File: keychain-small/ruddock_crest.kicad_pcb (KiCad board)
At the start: 2 copper layers, 38.1 x 45.7 mm, 4 parts

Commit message: Migrate to KiCad 5.1.4
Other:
- outline, holes or cut-outs redrawn
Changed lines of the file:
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@@
-(kicad_pcb (version 20171130) (host pcbnew "(5.0.1)-3")
+(kicad_pcb (version 20171130) (host pcbnew "(5.1.4)-1")
   (general
     (thickness 1.6)
@@
     (zone_45_only no)
     (trace_min 0.2)
-    (segment_width 0.5)
-    (edge_width 0.1)
     (via_size 0.8)
     (via_drill 0.4)
@@
     (uvia_min_size 0.2)
     (uvia_min_drill 0.1)
+    (edge_width 0.1)
+    (segment_width 0.5)
     (pcb_text_width 0.3)
     (pcb_text_size 1.5 1.5)
@@
       (xy 0.287869 -18.341347)) (layer F.Cu) (width 0.01))
   )
+  (gr_arc (start 140.97 107.95) (end 133.466674 90.423999) (angle -313.6458442) (layer Edge.Cuts) (width 0.1))
   (gr_arc (start 150.510695 85.344) (end 148.300896 90.576399) (angle 67.1) (layer B.SilkS) (width 0.5))
   (gr_arc (start 150.495 85.344) (end 148.285201 90.576399) (angle 67.1) (layer F.SilkS) (width 0.5))
@@
   (gr_arc (start 131.445 85.344) (end 133.984999 90.423999) (angle -63.4) (layer B.SilkS) (width 0.5))
   (gr_arc (start 131.445 85.344) (end 133.984999 90.423999) (angle -63.4) (layer F.SilkS) (width 0.5))
-  (gr_arc (start 140.97 107.95) (end 133.477001 90.424001) (angle -313.703074) (layer Edge.Cuts) (width 0.1))
-  (gr_arc (start 150.495 85.344) (end 148.463001 90.423999) (angle 68.2) (layer Edge.Cuts) (width 0.1))
+  (gr_arc (start 150.505326 85.344134) (end 148.473327 90.424133) (angle 68.2) (layer Edge.Cuts) (width 0.1))
   (gr_circle (center 150.495 85.344) (end 150.368 85.344) (layer Dwgs.User) (width 0.1))
   (gr_circle (center 150.495 85.344) (end 145.034 85.344) (layer Dwgs.User) (width 0.1))
-  (gr_arc (start 131.445 85.344) (end 133.476999 90.423999) (angle -68.19859051) (layer Edge.Cuts) (width 0.1))
+  (gr_arc (start 131.434674 85.343999) (end 133.466673 90.423998) (angle -68.19859051) (layer Edge.Cuts) (width 0.1))
   (gr_circle (center 131.445 85.344) (end 131.572 85.344) (layer Dwgs.User) (width 0.1))
   (gr_circle (center 131.445 85.344) (end 136.906 85.344) (layer Dwgs.User) (width 0.1))

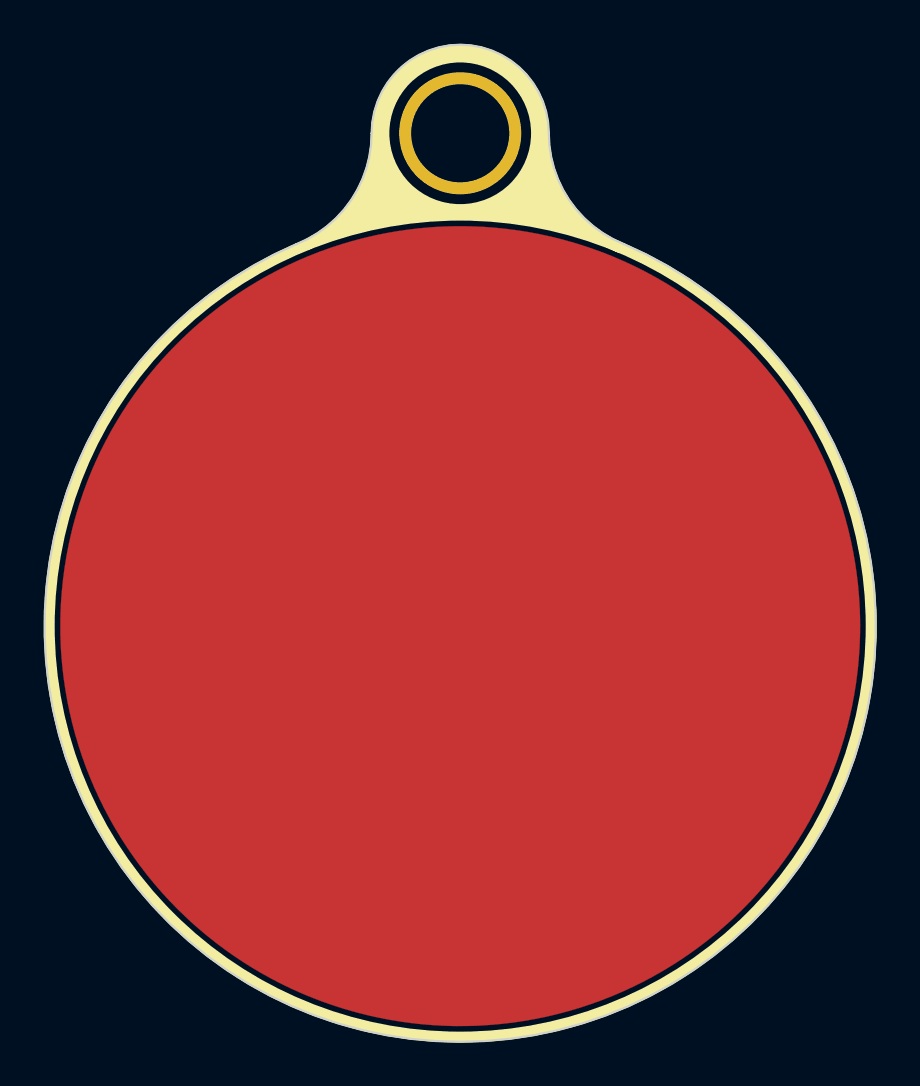
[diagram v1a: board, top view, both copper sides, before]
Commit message: Replace copper crest pad with fill zones
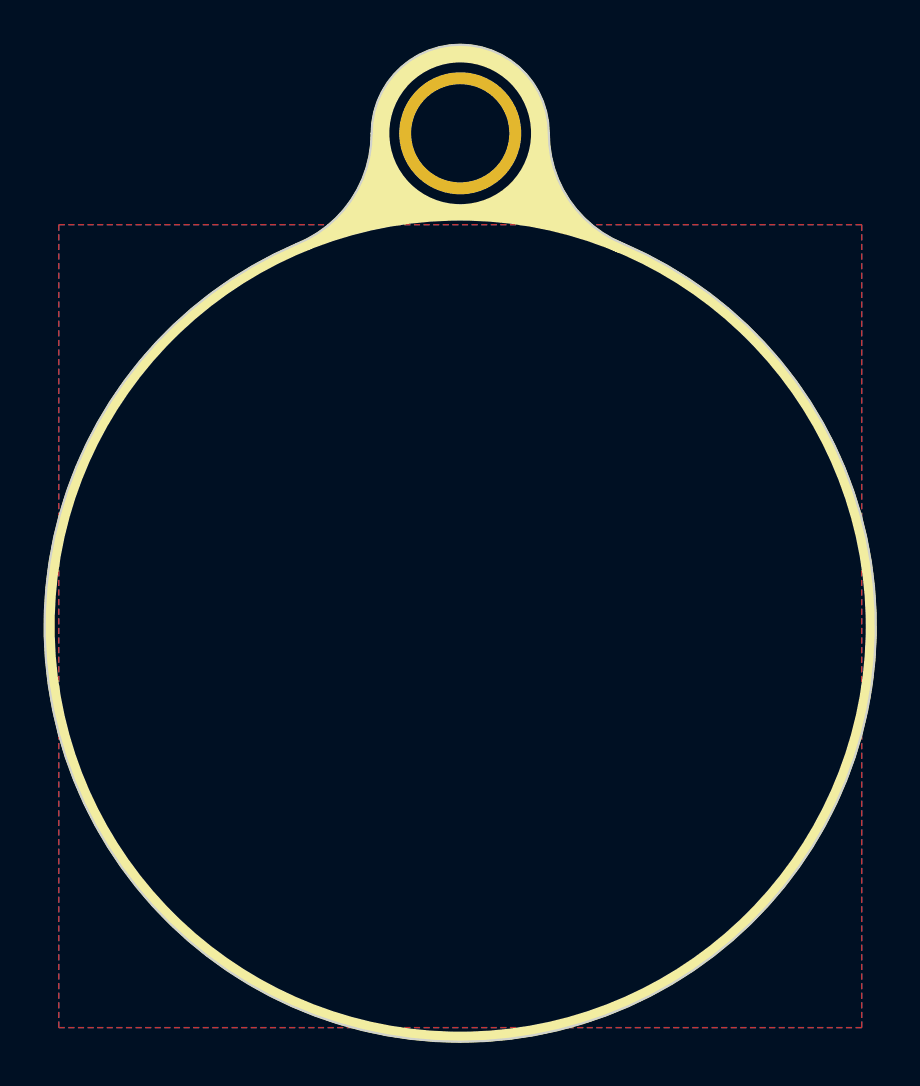
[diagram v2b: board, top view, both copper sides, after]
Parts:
- removed the G*** at (141.0, 108.0)
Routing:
- added copper zone on B.Cu, net (none)
- added copper zone on F.Cu, net (none)
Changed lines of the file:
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@@
     (tracks 0)
     (zones 0)
-    (modules 4)
+    (modules 3)
     (nets 1)
   )
@@
       (xy 9.730745 -13.40817) (xy 9.745385 -13.421618) (xy 9.978417 -13.636419) (xy 10.013345 -13.51111)) (layer F.Mask) (width 0.01))
   )
-  (module crest:circle_cu_1in5 (layer F.Cu)
-    (at 140.97 107.95)
-    (fp_text reference G*** (at 0 0) (layer F.SilkS) hide
-      (effects (font (size 1.524 1.524) (thickness 0.3)))
-    )
-    (fp_text value LOGO (at 0.75 0) (layer F.SilkS) hide
-      (effects (font (size 1.524 1.524) (thickness 0.3)))
-    )
-    (fp_poly (pts (xy 0.287869 -18.341347) (xy 0.628456 -18.333307) (xy 0.961238 -18.319252) (xy 1.067536 -18.313358)
-      (xy 1.586336 -18.275505) (xy 2.102502 -18.223229) (xy 2.615773 -18.156636) (xy 3.125887 -18.075837)
-      (xy 3.632583 -17.980939) (xy 4.135602 -17.872049) (xy 4.63468 -17.749278) (xy 5.129559 -17.612732)
-      (xy 5.619975 -17.46252) (xy 6.10567 -17.29875) (xy 6.58638 -17.121531) (xy 7.061847 -16.930971)
-      (xy 7.531807 -16.727178) (xy 7.996001 -16.51026) (xy 8.454168 -16.280326) (xy 8.906046 -16.037484)
-      (xy 9.351375 -15.781841) (xy 9.789892 -15.513508) (xy 10.221339 -15.232591) (xy 10.645453 -14.939199)
-      (xy 11.061973 -14.63344) (xy 11.470638 -14.315423) (xy 11.871188 -13.985255) (xy 12.208452 -13.692138)
-      (xy 12.383032 -13.534063) (xy 12.563152 -13.366008) (xy 12.746398 -13.190385) (xy 12.930358 -13.009606)
-      (xy 13.11262 -12.826085) (xy 13.290771 -12.642233) (xy 13.462399 -12.460464) (xy 13.62509 -12.28319)
-      (xy 13.692138 -12.208453) (xy 14.033691 -11.813903) (xy 14.363246 -11.41087) (xy 14.680696 -10.999533)
-      (xy 14.985936 -10.580068) (xy 15.278857 -10.152652) (xy 15.559353 -9.717464) (xy 15.827317 -9.274679)
-      (xy 16.082642 -8.824475) (xy 16.325222 -8.367031) (xy 16.554949 -7.902522) (xy 16.771718 -7.431126)
-      (xy 16.97542 -6.95302) (xy 17.165949 -6.468382) (xy 17.189629 -6.405218) (xy 17.364087 -5.916258)
-      (xy 17.524449 -5.423109) (xy 17.67067 -4.925995) (xy 17.802701 -4.425139) (xy 17.920497 -3.920765)
-      (xy 18.024008 -3.413097) (xy 18.11319 -2.90236) (xy 18.187993 -2.388777) (xy 18.248372 -1.872571)
-      (xy 18.294279 -1.353968) (xy 18.313357 -1.067537) (xy 18.329376 -0.738224) (xy 18.339381 -0.399719)
-      (xy 18.343371 -0.056272) (xy 18.341346 0.287869) (xy 18.333306 0.628456) (xy 18.319251 0.961238)
-      (xy 18.313357 1.067536) (xy 18.275504 1.586336) (xy 18.223228 2.102502) (xy 18.156636 2.615773)
-      (xy 18.075836 3.125887) (xy 17.980938 3.632583) (xy 17.872049 4.135602) (xy 17.749277 4.63468)
-      (xy 17.612731 5.129559) (xy 17.462519 5.619975) (xy 17.298749 6.10567) (xy 17.12153 6.58638)
-      (xy 16.93097 7.061847) (xy 16.727177 7.531807) (xy 16.510259 7.996001) (xy 16.280325 8.454168)
-      (xy 16.037483 8.906046) (xy 15.781841 9.351375) (xy 15.513507 9.789892) (xy 15.23259 10.221339)
-      (xy 14.939198 10.645453) (xy 14.633439 11.061973) (xy 14.315422 11.470638) (xy 13.985254 11.871188)
-      (xy 13.692138 12.208452) (xy 13.534062 12.383032) (xy 13.366007 12.563152) (xy 13.190384 12.746398)
-      (xy 13.009605 12.930358) (xy 12.826084 13.11262) (xy 12.642232 13.290771) (xy 12.460463 13.462399)
-      (xy 12.283189 13.62509) (xy 12.208452 13.692138) (xy 11.814467 14.033183) (xy 11.411954 14.362284)
-      (xy 11.001147 14.679318) (xy 10.582275 14.98416) (xy 10.155572 15.276688) (xy 9.721268 15.55678)
-      (xy 9.279596 15.824312) (xy 8.830786 16.079161) (xy 8.37507 16.321204) (xy 7.91268 16.550318)
-      (xy 7.443848 16.76638) (xy 6.968805 16.969268) (xy 6.487783 17.158858) (xy 6.001014 17.335027)
-      (xy 5.508728 17.497652) (xy 5.011159 17.64661) (xy 4.508536 17.781779) (xy 4.505739 17.782489)
-      (xy 4.005732 17.901871) (xy 3.502761 18.007024) (xy 2.996576 18.097984) (xy 2.486931 18.174786)
-      (xy 1.973579 18.237465) (xy 1.456271 18.286059) (xy 0.934759 18.320601) (xy 0.688034 18.331996)
-      (xy 0.640369 18.333612) (xy 0.580731 18.335179) (xy 0.511147 18.336678) (xy 0.433639 18.338086)
-      (xy 0.350234 18.339384) (xy 0.262955 18.340551) (xy 0.173826 18.341565) (xy 0.084873 18.342407)
-      (xy -0.00188 18.343055) (xy -0.084409 18.343489) (xy -0.160688 18.343687) (xy -0.228695 18.34363)
-      (xy -0.286403 18.343296) (xy -0.331789 18.342665) (xy -0.338667 18.342515) (xy -0.769418 18.328007)
-      (xy -1.192714 18.305017) (xy -1.607212 18.273641) (xy -2.011574 18.233973) (xy -2.245508 18.206637)
-      (xy -2.761471 18.135255) (xy -3.273909 18.049632) (xy -3.782573 17.949882) (xy -4.287213 17.836119)
-      (xy -4.787579 17.708454) (xy -5.283421 17.567001) (xy -5.774491 17.411874) (xy -6.260539 17.243185)
-      (xy -6.741315 17.061048) (xy -7.216569 16.865575) (xy -7.686052 16.65688) (xy -8.149515 16.435076)
-      (xy -8.606707 16.200275) (xy -9.05738 15.952591) (xy -9.501284 15.692137) (xy -9.938169 15.419026)
-      (xy -10.367785 15.133371) (xy -10.789884 14.835285) (xy -11.204215 14.524881) (xy -11.61053 14.202273)
-      (xy -12.008577 13.867573) (xy -12.208453 13.692138) (xy -12.383033 13.534062) (xy -12.563152 13.366007)
-      (xy -12.746399 13.190384) (xy -12.930359 13.009605) (xy -13.112621 12.826084) (xy -13.290772 12.642232)
-      (xy -13.4624 12.460463) (xy -13.625091 12.283189) (xy -13.692138 12.208452) (xy -14.033691 11.813902)
-      (xy -14.363247 11.410869) (xy -14.680697 10.999532) (xy -14.985937 10.580067) (xy -15.278858 10.152652)
-      (xy -15.559354 9.717463) (xy -15.827318 9.274678) (xy -16.082643 8.824475) (xy -16.325223 8.36703)
-      (xy -16.55495 7.902521) (xy -16.771718 7.431125) (xy -16.975421 6.953019) (xy -17.16595 6.468381)
-      (xy -17.18963 6.405217) (xy -17.364088 5.916257) (xy -17.52445 5.423108) (xy -17.670671 4.925994)
-      (xy -17.802702 4.425138) (xy -17.920497 3.920764) (xy -18.024009 3.413097) (xy -18.11319 2.902359)
-      (xy -18.187994 2.388776) (xy -18.248373 1.872571) (xy -18.29428 1.353967) (xy -18.313358 1.067536)
-      (xy -18.329377 0.738223) (xy -18.339382 0.399718) (xy -18.343372 0.056271) (xy -18.341347 -0.28787)
-      (xy -18.333307 -0.628456) (xy -18.319252 -0.961239) (xy -18.313358 -1.067537) (xy -18.275505 -1.586337)
-      (xy -18.223229 -2.102503) (xy -18.156636 -2.615773) (xy -18.075837 -3.125888) (xy -17.980939 -3.632584)
-      (xy -17.872049 -4.135602) (xy -17.749278 -4.634681) (xy -17.612732 -5.129559) (xy -17.46252 -5.619976)
-      (xy -17.29875 -6.10567) (xy -17.121531 -6.586381) (xy -16.930971 -7.061847) (xy -16.727178 -7.531808)
-      (xy -16.51026 -7.996002) (xy -16.280326 -8.454169) (xy -16.037484 -8.906047) (xy -15.781841 -9.351375)
-      (xy -15.513508 -9.789893) (xy -15.232591 -10.22134) (xy -14.939199 -10.645453) (xy -14.63344 -11.061973)
-      (xy -14.315423 -11.470639) (xy -13.985255 -11.871189) (xy -13.692138 -12.208453) (xy -13.534063 -12.383033)
-      (xy -13.366008 -12.563152) (xy -13.190385 -12.746399) (xy -13.009606 -12.930359) (xy -12.826085 -13.112621)
-      (xy -12.642233 -13.290772) (xy -12.460464 -13.4624) (xy -12.28319 -13.625091) (xy -12.208453 -13.692138)
-      (xy -11.813903 -14.033691) (xy -11.41087 -14.363247) (xy -10.999533 -14.680697) (xy -10.580068 -14.985937)
-      (xy -10.152652 -15.278858) (xy -9.717464 -15.559354) (xy -9.274679 -15.827318) (xy -8.824475 -16.082643)
-      (xy -8.367031 -16.325223) (xy -7.902522 -16.55495) (xy -7.431126 -16.771718) (xy -6.95302 -16.975421)
-      (xy -6.468382 -17.16595) (xy -6.405218 -17.18963) (xy -5.916258 -17.364088) (xy -5.423109 -17.52445)
-      (xy -4.925995 -17.670671) (xy -4.425139 -17.802702) (xy -3.920765 -17.920497) (xy -3.413097 -18.024009)
-      (xy -2.90236 -18.11319) (xy -2.388777 -18.187994) (xy -1.872571 -18.248373) (xy -1.353968 -18.29428)
-      (xy -1.067537 -18.313358) (xy -0.738224 -18.329377) (xy -0.399719 -18.339382) (xy -0.056272 -18.343372)
-      (xy 0.287869 -18.341347)) (layer F.Cu) (width 0.01))
-  )
   (gr_arc (start 140.97 107.95) (end 133.466674 90.423999) (angle -313.6458442) (layer Edge.Cuts) (width 0.1))
   (gr_arc (start 150.510695 85.344) (end 148.300896 90.576399) (angle 67.1) (layer B.SilkS) (width 0.5))
@@
   (gr_circle (center 140.97 107.95) (end 159.82 107.95) (layer F.SilkS) (width 0.5))
   (gr_circle (center 140.97 107.95) (end 140.97 88.9) (layer Dwgs.User) (width 0.1))
+  (zone (net 0) (net_name "") (layer F.Cu) (hatch edge 0.508)
+    (connect_pads (clearance 0.508))
+    (min_thickness 0.254)
+    (fill yes (arc_segments 32) (thermal_gap 0.508) (thermal_bridge_width 0.508) (smoothing fillet) (radius 19))
+    (polygon
+      (pts
+        (xy 122.555 89.535) (xy 122.555 126.365) (xy 159.385 126.365) (xy 159.385 89.535)
+      )
+    )
+  )
+  (zone (net 0) (net_name "") (layer B.Cu) (hatch edge 0.508)
+    (connect_pads (clearance 0.508))
+    (min_thickness 0.254)
+    (fill yes (arc_segments 32) (thermal_gap 0.508) (thermal_bridge_width 0.508) (smoothing fillet) (radius 19))
+    (polygon
+      (pts
+        (xy 122.555 89.535) (xy 159.385 89.535) (xy 159.385 126.365) (xy 122.555 126.365)
+      )
+    )
+  )
 )
